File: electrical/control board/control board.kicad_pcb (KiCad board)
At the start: 4 copper layers, 72.4 x 149.8 mm, 50 parts, among them J1 analog_extra, J10 Motor_2, J11 Motor_3, J12 Motor_4, J13 Motor_5, J14 Motor_6, J15 Motor_7, J16 Motor_8, J2 Programming_Header, J3 Conn_01x08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

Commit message: Found parts for LEDs
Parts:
- added C15: .1uF, Capacitor_SMD:C_0603_1608Metric_Pad1.05x0.95mm_HandSolder, B.Cu at (157.8, 63.5)
- added C17: .1uF, Capacitor_SMD:C_0603_1608Metric_Pad1.05x0.95mm_HandSolder, F.Cu at (147.6, 77.4)
- added C18: .1uF, Capacitor_SMD:C_0603_1608Metric_Pad1.05x0.95mm_HandSolder, B.Cu at (162.2, 63.5)
- added U7: ICM20648, footprints:ICM-20648, F.Cu at (148.1, 74.5)
- added Y1: 8Mhz, Crystal:Crystal_HC49-U_Vertical, B.Cu at (76.8, 101.0)
- C2, C3: moved to B.Cu
- moved C3 101.4 mm to (71.8, 106.3), turned to 270 degrees
- moved C2 93.3 mm to (77.5, 106.3), turned to 270 degrees
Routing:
- net Net-(C2-Pad1): track 0.00 -> 29.0 mm, vias 0 -> 1
- net Net-(C3-Pad1): track 0.00 -> 25.8 mm, vias 0 -> 1
- net GND: track 33.6 -> 34.7 mm, vias 19 -> 21
- net Net-(J5-Pad3): track 80.9 -> 81.5 mm

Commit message: leds are sort of aded
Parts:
- added D1: LED-RED, LED_SMD:LED_0603_1608Metric_Pad1.05x0.95mm_HandSolder, B.Cu at (56.3, 101.6)
- added D2: LED-YELLOW, LED_SMD:LED_0603_1608Metric_Pad1.05x0.95mm_HandSolder, B.Cu at (56.3, 105.4)
- added D3: LED-GREEN, LED_SMD:LED_0603_1608Metric_Pad1.05x0.95mm_HandSolder, B.Cu at (56.3, 109.2)
- added D4: LED-RED, LED_SMD:LED_0603_1608Metric_Pad1.05x0.95mm_HandSolder, B.Cu at (58.0, 122.6)
- added D5: LED-YELLOW, LED_SMD:LED_0603_1608Metric_Pad1.05x0.95mm_HandSolder, B.Cu at (58.0, 125.7)
- added D6: LED-GREEN, LED_SMD:LED_0603_1608Metric_Pad1.05x0.95mm_HandSolder, B.Cu at (58.2, 128.9)
- R10, R11, R17, R18, R19, R9: moved to B.Cu
- moved R19 130.1 mm to (53.3, 128.9), turned to 180 degrees
- moved R17 127.3 mm to (53.3, 122.6), turned to 180 degrees
- moved R18 124.7 mm to (53.3, 125.7), turned to 180 degrees
- moved R10 113.6 mm to (60.6, 105.4)
- moved R11 111.1 mm to (60.6, 109.2)
- moved R9 108.0 mm to (60.6, 101.6), turned to 180 degrees

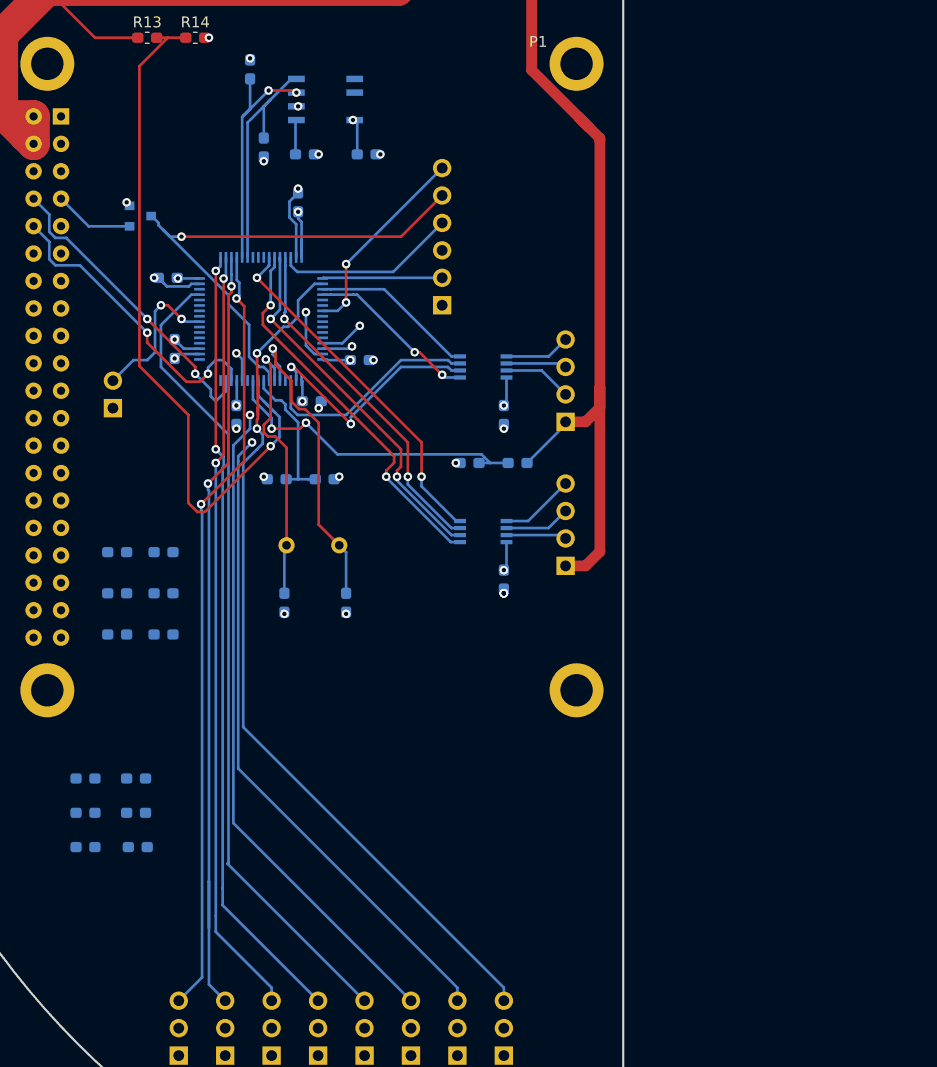
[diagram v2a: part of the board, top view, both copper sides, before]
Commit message: destoryed a lot of stuff around the microcontroller
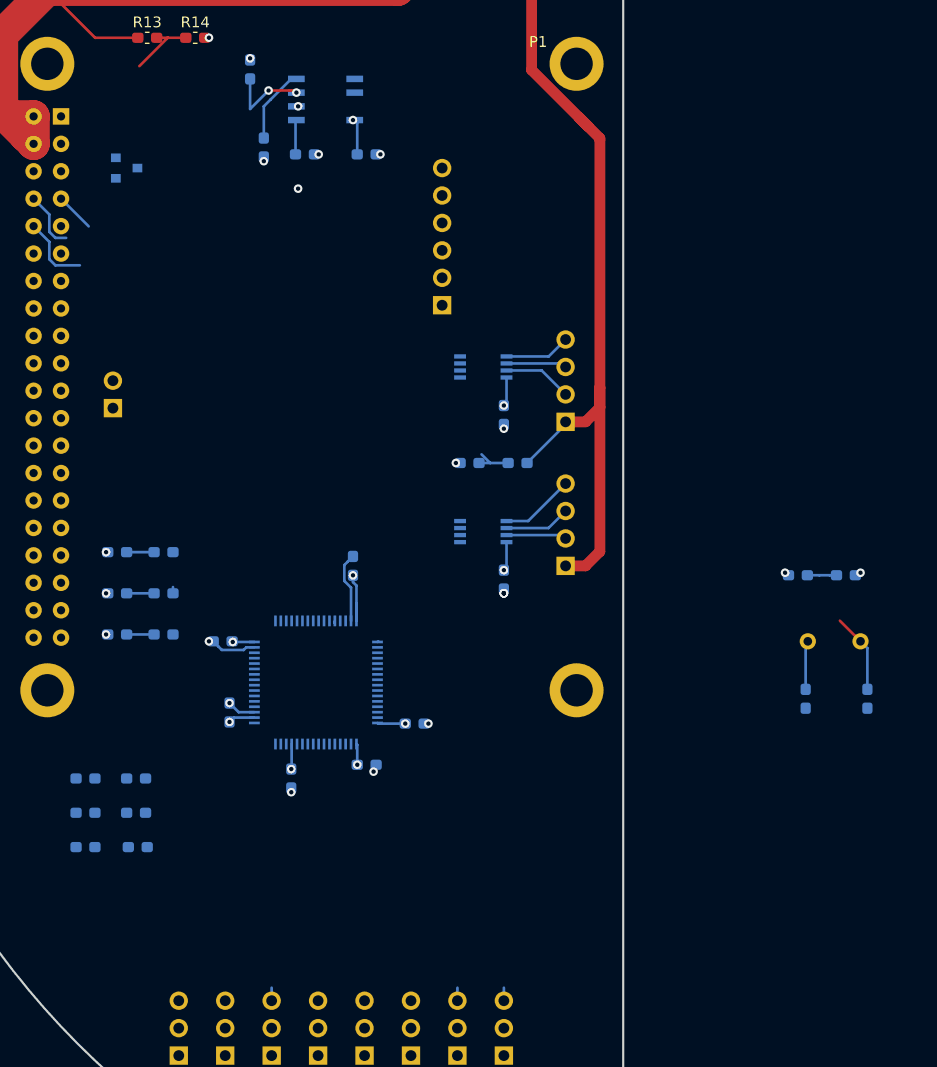
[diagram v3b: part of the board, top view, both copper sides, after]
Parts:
- moved C2 49.1 mm to (125.7, 115.2)
- moved C3 49.1 mm to (120.0, 115.2)
- moved R7 49.1 mm to (119.3, 103.7)
- moved Y1 49.1 mm to (125.1, 109.9)
- moved R8 49.1 mm to (123.7, 103.7)
- moved C6 34.0 mm to (66.0, 109.9)
- moved C10 34.0 mm to (83.8, 117.5)
- moved C5 34.0 mm to (78.1, 102.9)
- moved C8 34.0 mm to (72.4, 122.6)
- moved C9 34.0 mm to (79.4, 121.3)
- moved U1 34.0 mm to (74.7, 113.7)
- moved C7 34.0 mm to (66.7, 116.4)
- moved Q2 4.62 mm to (57.1, 66.0)
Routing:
- net Net-(J10-Pad3): track 82.4 -> 1.20 mm, vias 2 -> 0
- net Net-(J5-Pad3): track 81.5 -> 1.20 mm, vias 2 -> 0
- net Net-(J11-Pad3): track 76.6 -> 0.00 mm, vias 2 -> 0
- net Net-(J12-Pad3): track 75.2 -> 0.00 mm
- net Net-(J15-Pad3): track 74.7 -> 0.00 mm, vias 2 -> 0
- net Net-(J13-Pad3): track 73.9 -> 0.00 mm, vias 2 -> 0
- net Net-(J16-Pad3): track 71.9 -> 0.00 mm, vias 2 -> 0
- net Net-(J14-Pad3): track 71.4 -> 1.20 mm, vias 2 -> 0
- net /5V_MEASURE: track 67.9 -> 6.41 mm, vias 1 -> 0
- net /NRST: track 47.7 -> 0.00 mm, vias 1 -> 0
- net /SENSOR_RX: track 35.5 -> 0.00 mm, vias 2 -> 0
- net /SENSOR_RE: track 34.1 -> 0.18 mm, vias 2 -> 0
- net /SENSOR_TX: track 32.9 -> 0.35 mm, vias 2 -> 0
- net /SENSOR_DE: track 32.3 -> 0.00 mm, vias 2 -> 0
- net /48V_MEASURE: track 29.9 -> 3.83 mm, vias 2 -> 0
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
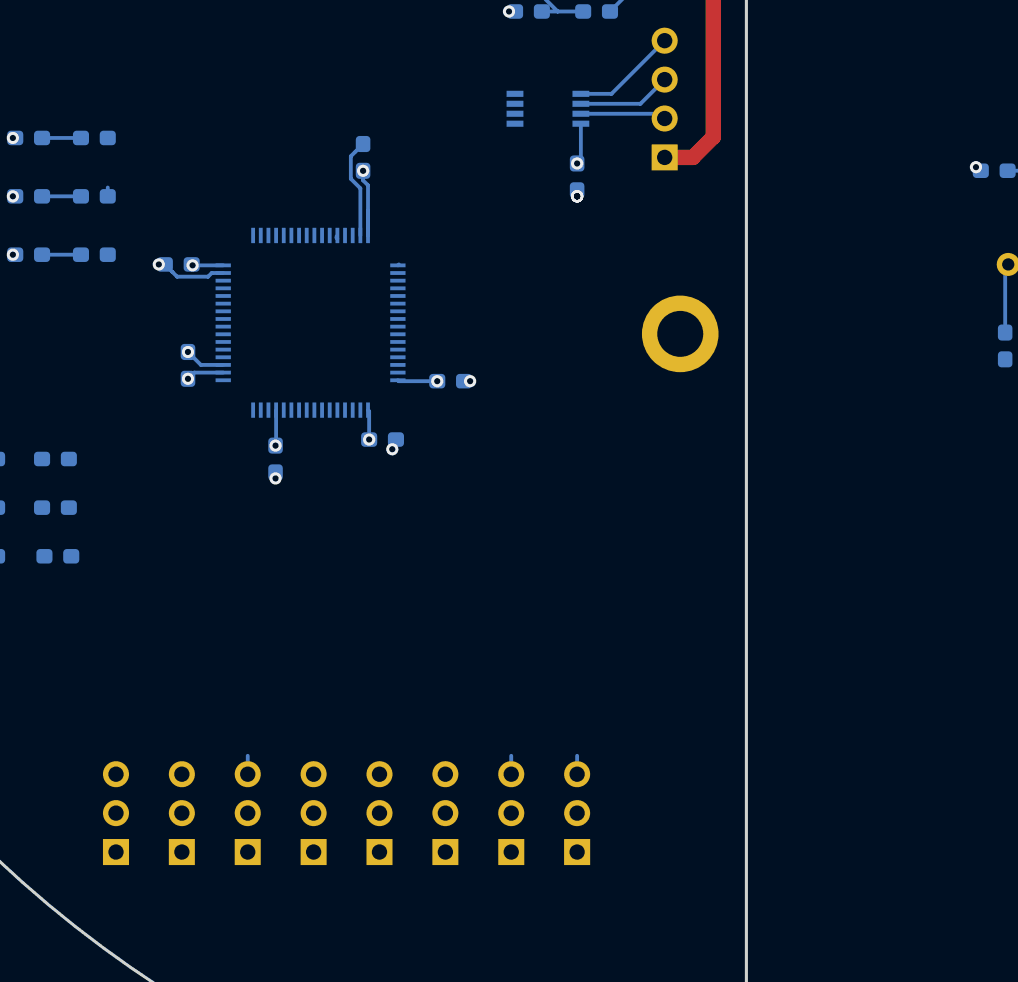
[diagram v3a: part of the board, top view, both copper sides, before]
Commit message: Changed pins on motors
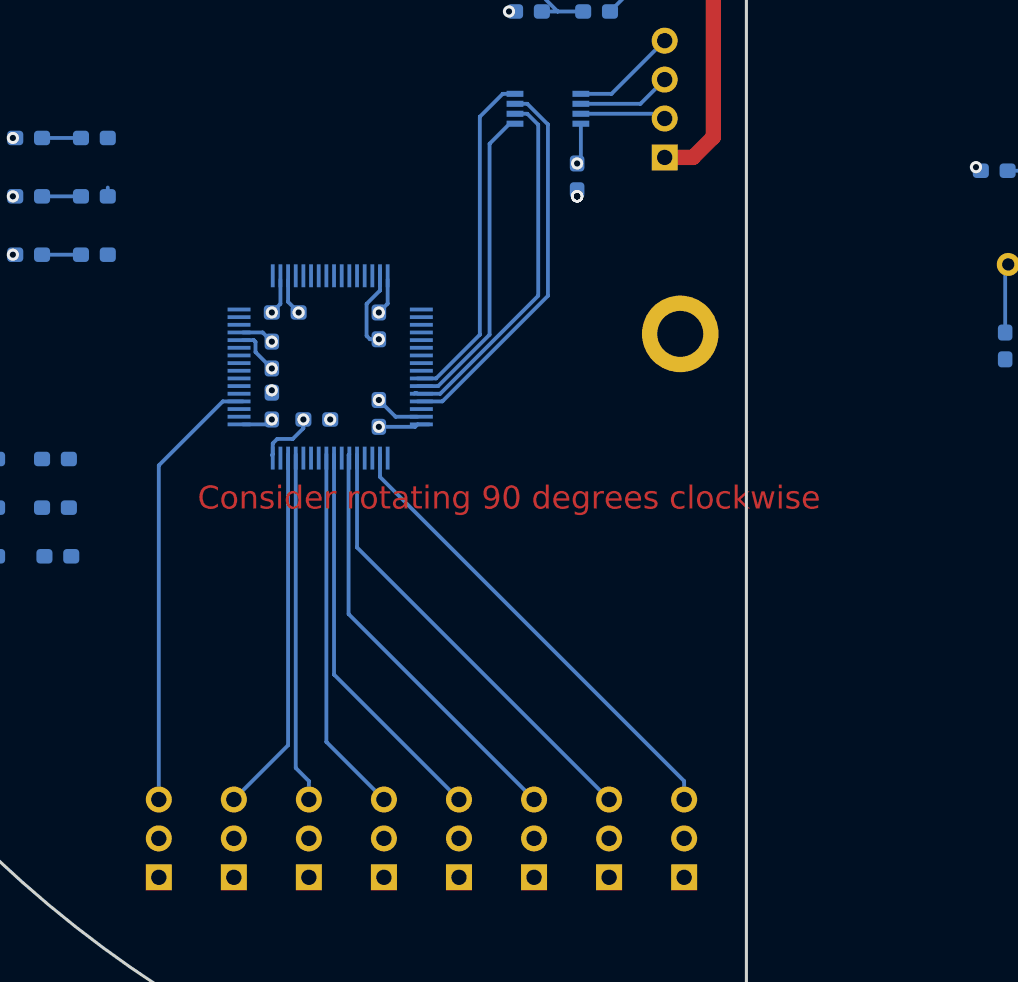
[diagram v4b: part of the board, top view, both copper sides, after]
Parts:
- U1: footprint Package_QFP:LQFP-64_10x10mm_P0.5mm -> footprints:LQFP-64_10x10mm_P0.5mm_handsolder
- moved J16 37.1 mm to (99.1, 149.9)
- moved J15 27.9 mm to (94.2, 149.9)
- moved J5 27.4 mm to (64.8, 149.9)
- moved J14 18.8 mm to (89.3, 149.9)
- moved J10 18.2 mm to (69.7, 149.9)
- moved C5 16.7 mm to (79.1, 119.6)
- moved C6 13.7 mm to (79.1, 113.9), turned to 90 degrees
- moved J13 9.63 mm to (84.4, 149.9)
- moved C10 9.09 mm to (75.1, 120.0)
- moved J11 9.06 mm to (74.6, 149.9)
- moved C9 7.55 mm to (72.1, 119.1), turned to 270 degrees
- moved C7 7.23 mm to (73.0, 113.0), turned to 0 degrees
- moved C8 6.79 mm to (72.1, 115.8)
- moved U1 3.15 mm to (76.0, 116.5), turned to 0 degrees
- moved J12 1.68 mm to (79.5, 149.9)
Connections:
- J10 pad 3: Net-(J10-Pad3) -> /MOTOR_2
- J11 pad 3: Net-(J11-Pad3) -> /MOTOR_3
- J12 pad 3: Net-(J12-Pad3) -> /MOTOR_4
- J13 pad 3: Net-(J13-Pad3) -> /MOTOR_5
- J14 pad 3: Net-(J14-Pad3) -> /MOTOR_6
- J15 pad 3: Net-(J15-Pad3) -> /MOTOR_7
- J16 pad 3: Net-(J16-Pad3) -> /MOTOR_8
- J5 pad 3: Net-(J5-Pad3) -> /MOTOR_1
- U1 pad 28: /SWITCH_C -> Net-(U1-Pad28)
- U1 pad 29: Net-(J12-Pad3) -> Net-(U1-Pad29)
- U1 pad 33: Net-(J13-Pad3) -> Net-(U1-Pad33)
- U1 pad 34: Net-(J14-Pad3) -> Net-(U1-Pad34)
- U1 pad 35: Net-(J15-Pad3) -> Net-(U1-Pad35)
- U1 pad 36: Net-(J16-Pad3) -> Net-(U1-Pad36)
- U1 pad 4: Net-(U1-Pad4) -> /MOTOR_1
- U1 pad 50: Net-(J5-Pad3) -> /MOTOR_8
- U1 pad 53: Net-(U1-Pad53) -> /MOTOR_7
- U1 pad 54: Net-(U1-Pad54) -> /MOTOR_6
- U1 pad 56: /SWITCH_D -> /MOTOR_5
- U1 pad 57: Net-(U1-Pad57) -> /MOTOR_4
- U1 pad 61: Net-(J10-Pad3) -> /MOTOR_3
- U1 pad 62: Net-(J11-Pad3) -> /MOTOR_2
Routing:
- net /MOTOR_8: track 0.00 -> 30.8 mm
- net /MOTOR_7: track 0.00 -> 29.3 mm
- net /MOTOR_1: track 0.00 -> 29.0 mm
- net /MOTOR_6: track 0.00 -> 27.6 mm
- net /MOTOR_5: track 0.00 -> 25.9 mm
- net /SENSOR_DE: track 0.00 -> 25.3 mm
- net /MOTOR_4: track 0.00 -> 24.1 mm
- net /MOTOR_2: track 0.00 -> 24.0 mm
- net /SENSOR_RE: track 0.18 -> 23.7 mm
- net /MOTOR_3: track 0.00 -> 22.9 mm
- net /SENSOR_TX: track 0.35 -> 22.7 mm
- net /SENSOR_RX: track 0.00 -> 20.8 mm
- net +3V3: track 26.2 -> 24.8 mm
- net Net-(J5-Pad3): track 1.20 -> 0.00 mm
- net Net-(J14-Pad3): track 1.20 -> 0.00 mm
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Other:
- board text added: "Consider rotating 90 degrees clockwise"

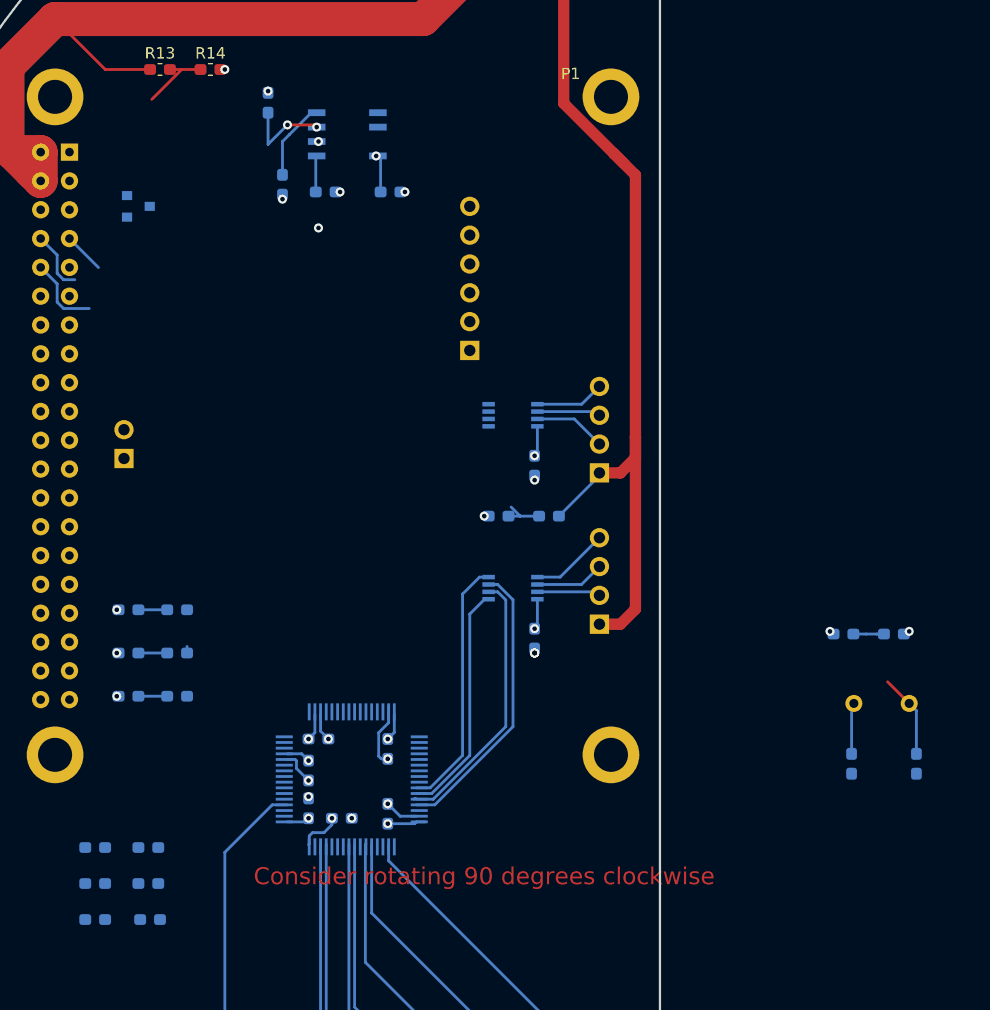
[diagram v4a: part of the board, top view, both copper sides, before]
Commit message: board is mostly routed
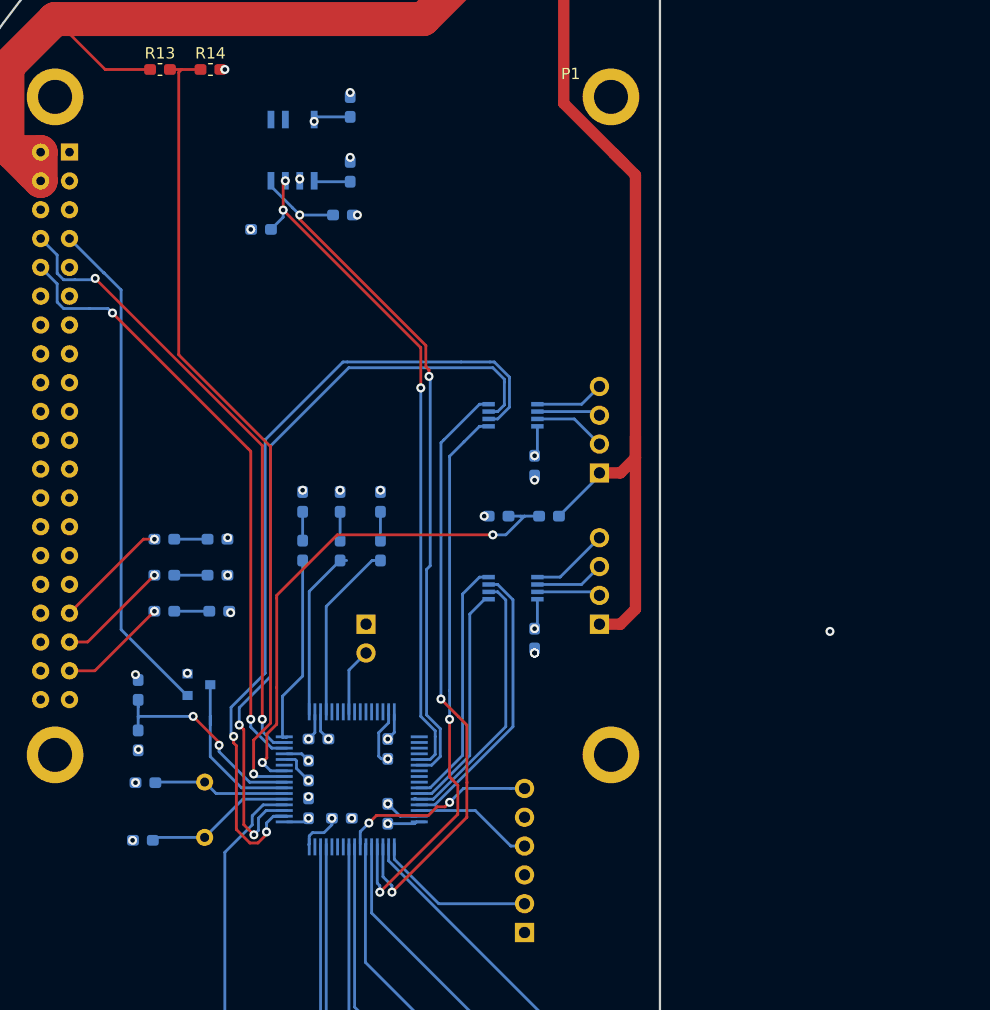
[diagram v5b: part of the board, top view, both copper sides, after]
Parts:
- moved C2 68.5 mm to (57.5, 121.9), turned to 180 degrees
- moved R8 66.8 mm to (57.1, 108.7), turned to 90 degrees
- moved Y1 63.2 mm to (63.0, 121.7), turned to 90 degrees
- moved R7 62.9 mm to (57.1, 113.1), turned to 90 degrees
- moved C3 62.3 mm to (57.8, 116.8), turned to 180 degrees
- moved J2 51.5 mm to (91.2, 130.0)
- moved Q2 42.5 mm to (62.5, 108.2)
- moved D3 28.0 mm to (78.5, 92.1), turned to 270 degrees
- moved D4 27.9 mm to (64.1, 95.4)
- moved R17 27.9 mm to (59.4, 95.4)
- moved D5 27.9 mm to (64.1, 98.6)
- moved D6 27.9 mm to (64.3, 101.7)
- moved R18 27.9 mm to (59.4, 98.6)
- moved R19 27.9 mm to (59.4, 101.7)
- moved J1 25.9 mm to (77.2, 102.9), turned to 180 degrees
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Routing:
- net /MISC_RE: track 0.00 -> 73.2 mm, vias 0 -> 2
- net /MISC_DE: track 0.00 -> 68.2 mm, vias 0 -> 2
- net /5V_MEASURE: track 6.41 -> 71.9 mm, vias 0 -> 1
- net /HIH_SDA: track 7.00 -> 62.6 mm, vias 0 -> 2
- net /MISC_TX: track 0.00 -> 53.5 mm, vias 0 -> 2
- net /HIH_SCL: track 7.86 -> 60.2 mm, vias 2 -> 3
- net /MISC_RX: track 0.00 -> 50.8 mm, vias 0 -> 2
- net /ODROID_TX: track 5.46 -> 55.9 mm, vias 0 -> 2
- net /ODROID_RX: track 6.73 -> 54.5 mm, vias 0 -> 2
- net /48V_MEASURE: track 3.83 -> 45.2 mm, vias 0 -> 2
- net /STM_RESET: track 3.62 -> 44.6 mm
- net /JTDO: track 0.00 -> 17.1 mm, vias 0 -> 2
- net Net-(R9-Pad1): track 0.00 -> 16.8 mm
- net /3.3V_MEASURE: track 2.69 -> 18.7 mm, vias 0 -> 2
- net Net-(R11-Pad2): track 0.00 -> 16.0 mm
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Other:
- board text removed: "Consider rotating 90 degrees clockwise"

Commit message: control board is almost finished
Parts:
- removed R12, R3, R4, R5: 10k, Resistor_SMD:R_0603_1608Metric_Pad1.05x0.95mm_HandSolder
- C17, U7: moved to B.Cu
- moved C18 77.4 mm to (98.0, 106.8), turned to 270 degrees
- moved C15 74.6 mm to (99.2, 109.7)
- moved C17 64.5 mm to (94.4, 113.8)
- moved U7 64.2 mm to (94.3, 109.6), turned to 270 degrees
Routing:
- net /NRST: track 15.0 -> 52.3 mm, vias 0 -> 1
- net /ICM_SCL: track 0.00 -> 24.5 mm, vias 0 -> 2
- net /ICM_SDA: track 0.00 -> 19.6 mm, vias 0 -> 2
- net GND: track 27.1 -> 39.1 mm, vias 26 -> 31
- net +3V3: track 24.8 -> 33.5 mm, vias 12 -> 15
- net Net-(C15-Pad1): track 0.00 -> 2.56 mm
